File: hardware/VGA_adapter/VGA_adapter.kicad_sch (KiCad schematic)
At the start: 36 parts, among them J1 DF12NB(3.0)-30DS-0.5V(51), J2 DF12NB(3.0)-30DS-0.5V(51), J3 FPC Cable connector 1x15, U1 TXS0102DQMR

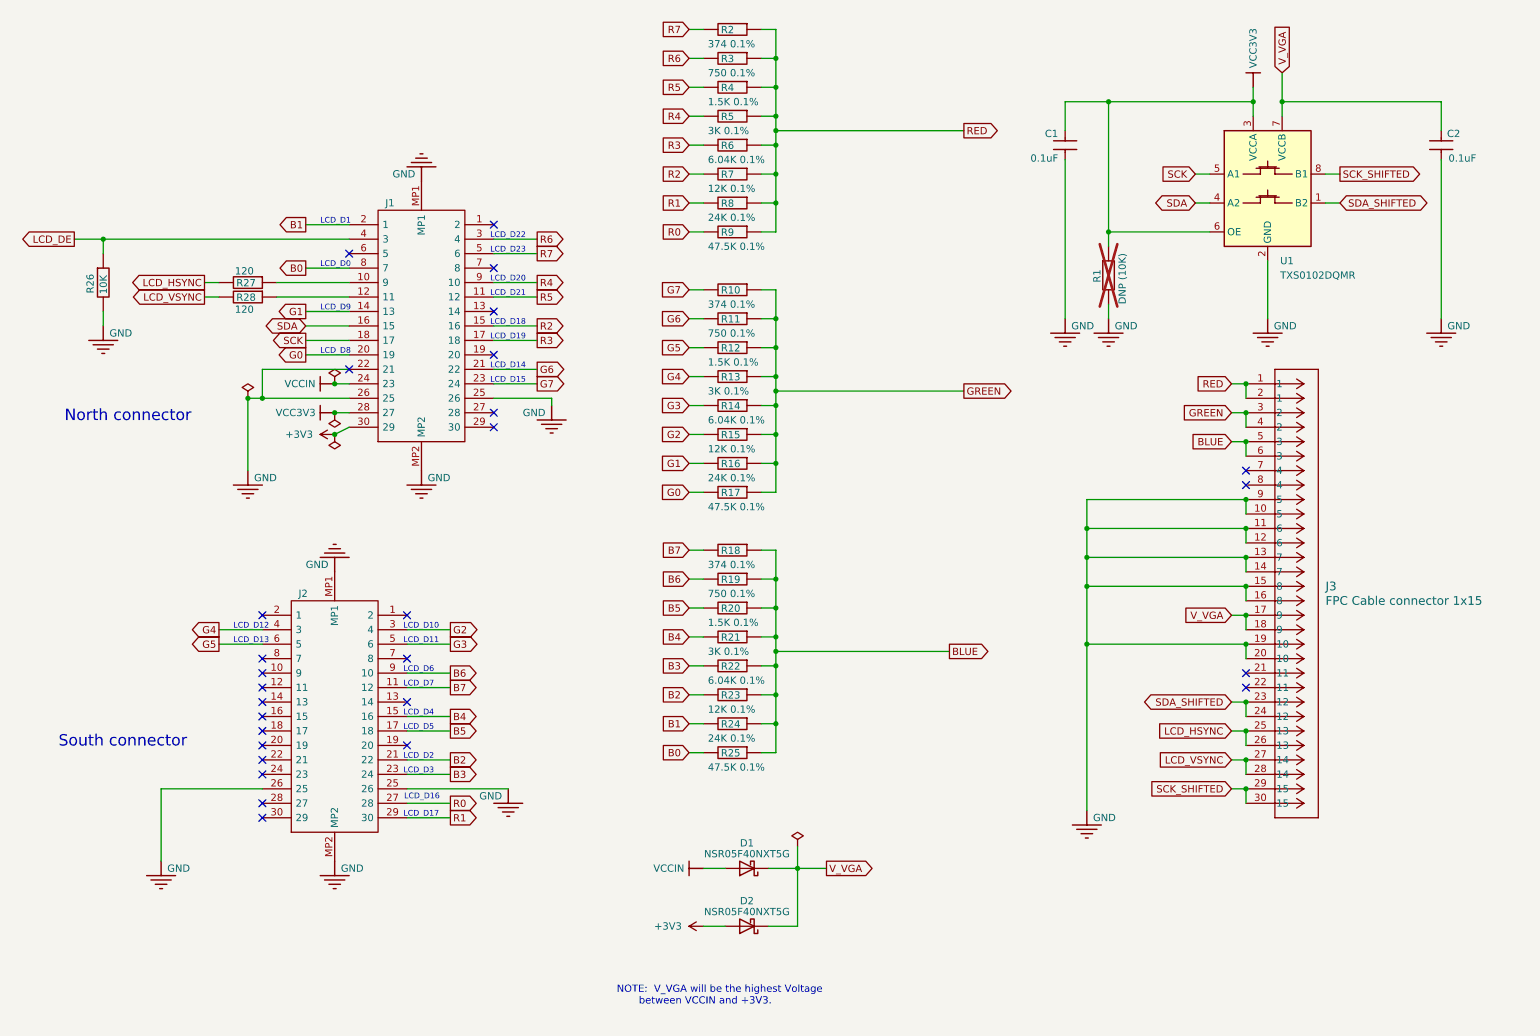
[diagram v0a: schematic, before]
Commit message: Fix transitors (correct is NMOS, fast version selected). Added charge pump. Fixed level translator pinout.
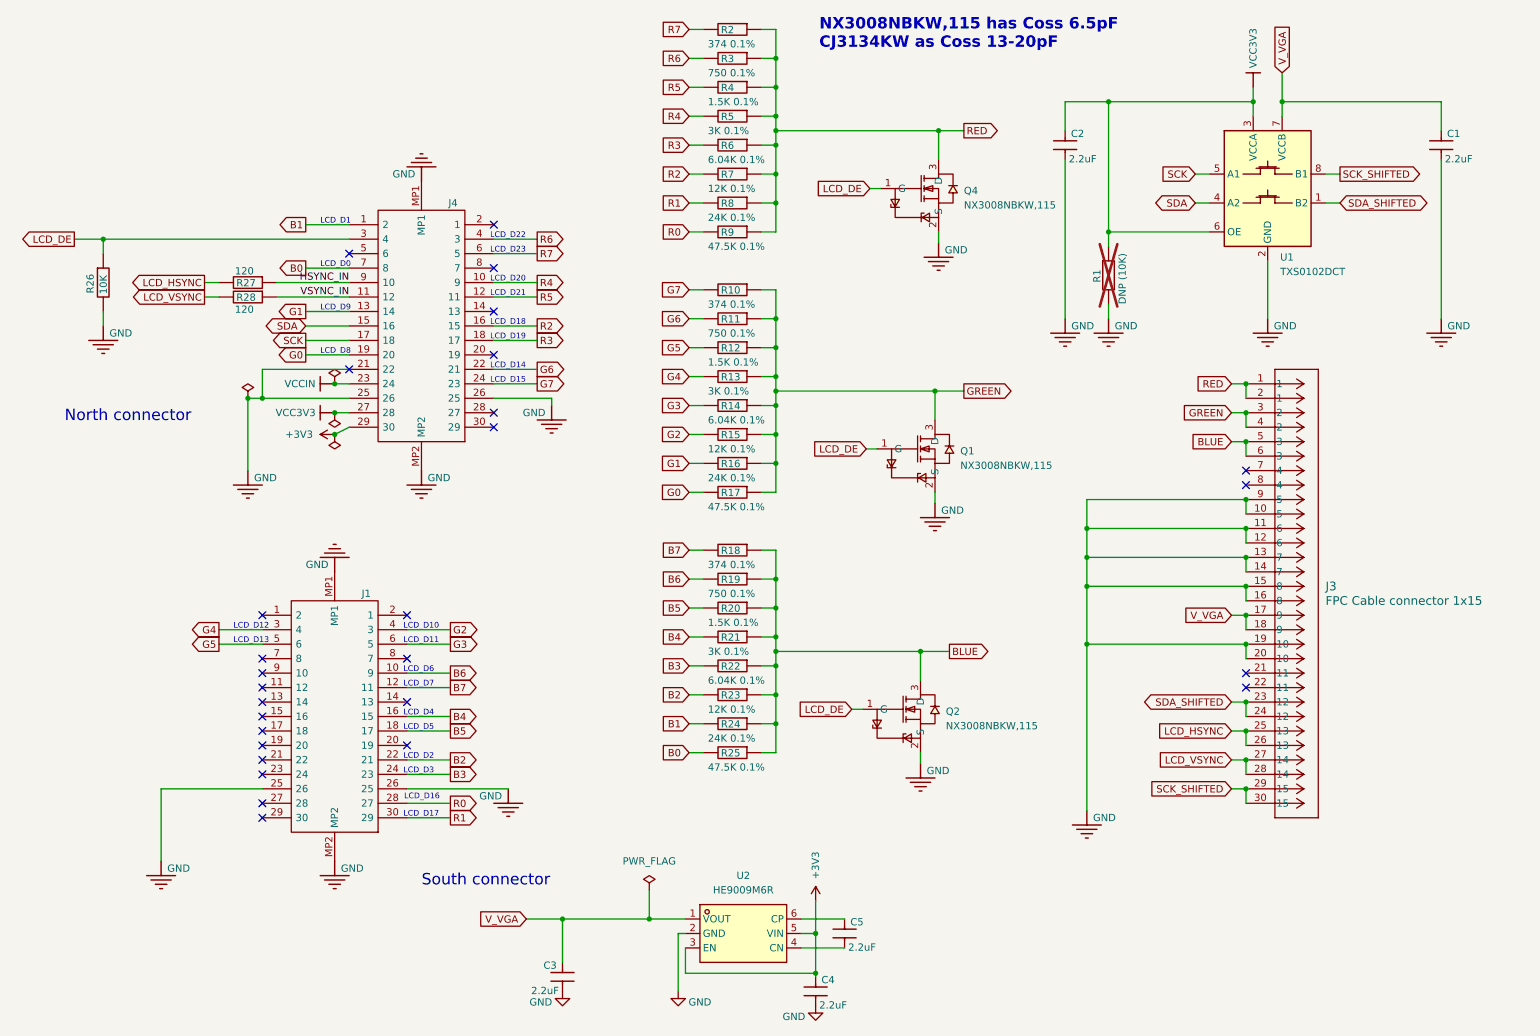
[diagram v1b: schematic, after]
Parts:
- removed D1, D2: NSR05F40NXT5G, Diode_SMD:D_0402_1005Metric, symbol Device:D_Schottky
- removed J2: DF12NB(3.0)-30DS-0.5V(51), DF12NB3030DP05V51, symbol DF12NB_3.0_-30DP-0.5V_51_:DF12NB_3.0_-30DP-0.5V_51_
- removed U1: TXS0102DQMR, Library:DQM8, symbol Logic_LevelTranslator:TXS0102DCU
- added C3, C4, C5: 2.2uF, Capacitor_SMD:C_0402_1005Metric, symbol Periph-altium-import:0_CAP
- added J4: DF12NB(3.0)-30DS-0.5V(51), easyeda2kicad:CONN-SMD_30P-P0.50_HRS_DF12NB-3.0-30DP-0.5V, symbol DF12NB_3.0_-30DP-0.5V_51_:DF12NB_3.0_-30DP-0.5V_51_
- added Q1, Q2, Q4: NX3008NBKW,115, easyeda2kicad:SOT-323-3_L2.0-W1.3-P1.30-LS2.1-BR, symbol easyeda2kicad:NX3008NBKW,115
- added U1: TXS0102DCT, Package_SO:SSOP-8_2.95x2.8mm_P0.65mm, symbol Logic_LevelTranslator:TXS0102DCT
- added U2: HE9009M6R, Package_TO_SOT_SMD:SOT-23-6, symbol easyeda2kicad:HE9009M6R
- C1, C2: value 0.1uF -> 2.2uF; footprint Library:C_0402_1005Metric -> Capacitor_SMD:C_0402_1005Metric; LCSC Part Number C60474 -> C170151
- J1: footprint DF12NB3030DP05V51 -> easyeda2kicad:CONN-SMD_30P-P0.50_HRS_DF12NB-3.0-30DP-0.5V; LCSC Part Number (none) -> C2904115
- J3: LCSC Part Number (none) -> C2922285
- R10, R18, R2: LCSC Part Number C852745 -> C2681606
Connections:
- net +3V3: now also C4.1, J4.29 (30), U2.3 (EN), U2.5 (VIN); no longer J1.30 (29)
- net B0: now also J4.7 (8); no longer J1.8 (7)
- net B1: now also J4.1 (2); no longer J1.2 (1)
- net B2: now also J1.22 (21)
- net B3: now also J1.24 (23)
- net B4: now also J1.16 (15)
- net B5: now also J1.18 (17)
- net B6: now also J1.10 (9)
- net B7: now also J1.12 (11)
- net BLUE: now also Q2.3 (D)
- net G0: now also J4.19 (20); no longer J1.20 (19)
- net G1: now also J4.13 (14); no longer J1.14 (13)
- net G2: now also J1.4 (3)
- net G3: now also J1.6 (5)
- net G4: now also J1.3 (4)
- net G5: now also J1.5 (6)
- net G6: now also J4.22 (21); no longer J1.21 (22)
- net G7: now also J4.24 (23); no longer J1.23 (24)
- net GND: now also C3.2, C4.2, J4.21 (22), J4.25 (26), J4.26 (25), J4.MP1, J4.MP2, Q1.2 (S), Q2.2 (S), Q4.2 (S), U1.2 (GND), U2.2 (GND); no longer J1.22 (21)
- net GREEN: now also Q1.3 (D)
- net LCD_DE: now also J4.3 (4), Q1.1 (G), Q2.1 (G), Q4.1 (G); no longer J1.4 (3)
- net R0: now also J1.28 (27)
- net R1: now also J1.30 (29)
- net R2: now also J4.16 (15); no longer J1.15 (16)
- net R3: now also J4.18 (17); no longer J1.17 (18)
- net R4: now also J4.10 (9); no longer J1.9 (10)
- net R5: now also J4.12 (11); no longer J1.11 (12)
- net R6: now also J4.4 (3); no longer J1.3 (4)
- net R7: now also J4.6 (5); no longer J1.5 (6)
- net RED: now also Q4.3 (D)
- net SCK: now also J4.17 (18), U1.5 (A1); no longer J1.18 (17)
- net SCK_SHIFTED: now also U1.8 (B1)
- net SDA: now also J4.15 (16), U1.4 (A2); no longer J1.16 (15)
- net SDA_SHIFTED: now also U1.1 (B2)
- net VCC3V3: now also C2.1, J4.27 (28), U1.3 (VCCA), U1.6 (OE); no longer C1.1, J1.28 (27)
- net VCCIN: now also J4.23 (24); no longer J1.24 (23)
- net V_VGA: now also C1.1, C3.1, U1.7 (VCCB), U2.1 (VOUT); no longer C2.1
- net HSYNC_IN: now reaches R27.1
- net HSYNC_IN: now also J4.9 (10); no longer J1.10 (9)
- net VSYNC_IN: now reaches R28.1
- net VSYNC_IN: now also J4.11 (12); no longer J1.12 (11)
- new net: C5.1, U2.6 (CP)
- new net: C5.2, U2.4 (CN)
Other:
- note added: "NX3008NBKW,115 has Coss 6.5pF CJ3134KW as Coss 13-20pF"
- note removed: "NOTE: V_VGA will be the highest Voltage between VCCIN and +3V3."

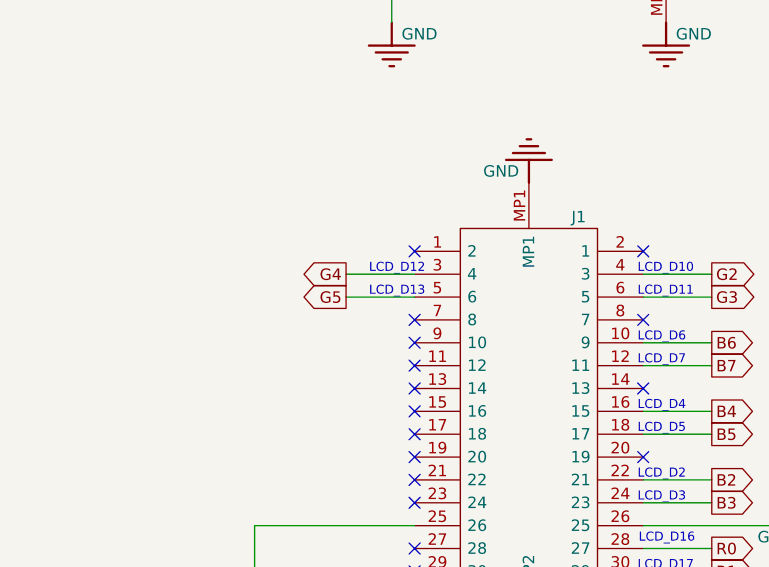
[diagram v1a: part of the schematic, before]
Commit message: fixed mixup of pins G5/G4 (3rd diff pair ODD) and DE/PCLK (3rd diff pair EVEN), now with correct polarity for diff pairs
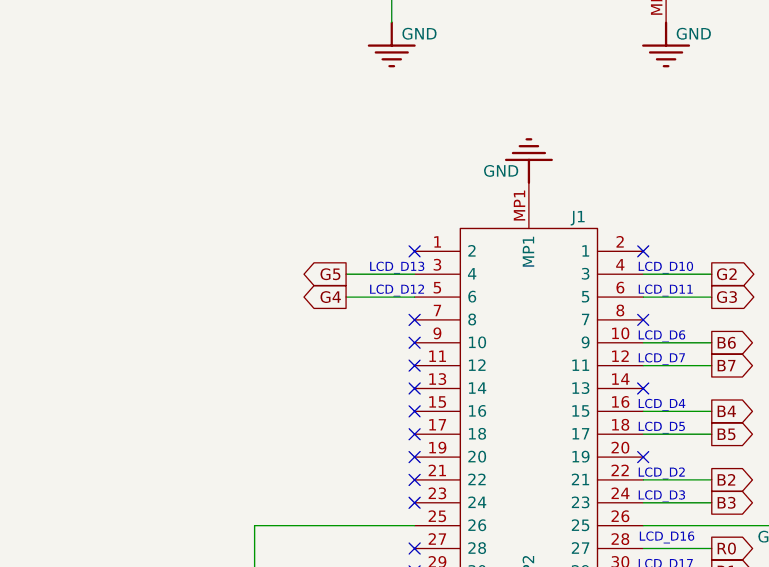
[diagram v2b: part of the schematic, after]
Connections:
- net G4: now also J1.5 (6); no longer J1.3 (4)
- net G5: now also J1.3 (4); no longer J1.5 (6)
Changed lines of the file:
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@@
+	(wire
+		(pts
+			(xy 57.15 128.27) (xy 64.77 128.27)
+		)
+		(stroke
+			(width 0.254)
+			(type default)
+		)
+	)
 	(wire
 		(pts
@@
 	(wire
 		(pts
-			(xy 57.15 128.27) (xy 64.77 128.27)
-		)
-		(stroke
-			(width 0.254)
-			(type default)
-		)
-	)
-	(wire
-		(pts
 			(xy 64.77 153.67) (xy 46.99 153.67)
 		)
@@
 	(wire
 		(pts
+			(xy 57.15 125.73) (xy 64.77 125.73)
+		)
+		(stroke
+			(width 0.254)
+			(type default)
+		)
+	)
+	(wire
+		(pts
 			(xy 152.4 96.52) (xy 154.94 96.52)
 		)
@@
 	(wire
 		(pts
-			(xy 57.15 125.73) (xy 64.77 125.73)
-		)
-		(stroke
-			(width 0.254)
-			(type default)
-		)
-	)
-	(wire
-		(pts
 			(xy 237.49 85.09) (xy 237.49 82.55)
 		)
@@
 		)
 	)
+	(text "LCD_D12"
+		(exclude_from_sim no)
+		(at 59.69 128.27 0)
+		(effects
+			(font
+				(size 1 1)
+			)
+			(justify left bottom)
+		)
+	)
 	(text "South connector"
 		(exclude_from_sim no)
@@
 		)
 	)
+	(text "LCD_D13"
+		(exclude_from_sim no)
+		(at 59.69 125.73 0)
+		(effects
+			(font
+				(size 1 1)
+			)
+			(justify left bottom)
+		)
+	)
 	(text "LCD_D11"
 		(exclude_from_sim no)
@@
 		(exclude_from_sim no)
 		(at 89.535 133.35 0)
-		(effects
-			(font
-				(size 1 1)
-			)
-			(justify left bottom)
-		)
-	)
-	(text "LCD_D13"
-		(exclude_from_sim no)
-		(at 59.69 128.27 0)
-		(effects
-			(font
-				(size 1 1)
-			)
-			(justify left bottom)
-		)
-	)
-	(text "LCD_D12"
-		(exclude_from_sim no)
-		(at 59.69 125.73 0)
 		(effects
 			(font
@@
 		)
 	)
+	(global_label "G5"
+		(shape output)
+		(at 57.15 125.73 180)
+		(fields_autoplaced yes)
+		(effects
+			(font
+				(size 1.27 1.27)
+			)
+			(justify right)
+		)
+		(property "Intersheetrefs" "${INTERSHEET_REFS}"
+			(at 51.6853 125.73 0)
+			(effects
+				(font
+					(size 1.27 1.27)
+				)
+				(justify right)
+				(hide yes)
+			)
+		)
+	)
 	(global_label "R7"
 		(shape input)
@@
 		(property "Intersheetrefs" "${INTERSHEET_REFS}"
 			(at 134.2353 20.32 0)
+			(effects
+				(font
+					(size 1.27 1.27)
+				)
+				(justify right)
+				(hide yes)
+			)
+		)
+	)
+	(global_label "G4"
+		(shape output)
+		(at 57.15 128.27 180)
+		(fields_autoplaced yes)
+		(effects
+			(font
+				(size 1.27 1.27)
+			)
+			(justify right)
+		)
+		(property "Intersheetrefs" "${INTERSHEET_REFS}"
+			(at 51.6853 128.27 0)
 			(effects
 				(font
@@
 		)
 	)
-	(global_label "G4"
-		(shape output)
-		(at 57.15 125.73 180)
-		(fields_autoplaced yes)
-		(effects
-			(font
-				(size 1.27 1.27)
-			)
-			(justify right)
-		)
-		(property "Intersheetrefs" "${INTERSHEET_REFS}"
-			(at 51.6853 125.73 0)
-			(effects
-				(font
-					(size 1.27 1.27)
-				)
-				(justify right)
-				(hide yes)
-			)
-		)
-	)
 	(global_label "R4"
 		(shape output)
@@
 				(hide yes)
 			)
-		)
-	)
-	(global_label "G5"
-		(shape output)
-		(at 57.15 128.27 180)
-		(fields_autoplaced yes)
-		(effects
-			(font
-				(size 1.27 1.27)
-			)
-			(justify right)
-		)
-		(property "Intersheetrefs" "${INTERSHEET_REFS}"
-			(at 51.6853 128.27 0)
-			(effects
-				(font
-					(size 1.27 1.27)
-				)
-				(justify right)
-				(hide yes)
-			)

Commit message: correct footprint of VGA adapter's level translator
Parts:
- removed U1: TXS0102DCT, Package_SO:SSOP-8_2.95x2.8mm_P0.65mm, symbol Logic_LevelTranslator:TXS0102DCT
- added U1: TXS0102DCU, Package_SO:VSSOP-8_2.3x2mm_P0.5mm, symbol Logic_LevelTranslator:TXS0102DCU
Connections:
- net GND: now also U1.2 (GND)
- net SCK: now also U1.5 (A1)
- net SCK_SHIFTED: now also U1.8 (B1)
- net SDA: now also U1.4 (A2)
- net SDA_SHIFTED: now also U1.1 (B2)
- net VCC3V3: now also U1.3 (VCCA), U1.6 (OE)
- net V_VGA: now also U1.7 (VCCB)
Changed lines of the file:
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@@
+	)
+	(symbol
+		(lib_id "Logic_LevelTranslator:TXS0102DCU")
+		(at 241.3 48.26 0)
+		(unit 1)
+		(exclude_from_sim no)
+		(in_bom yes)
+		(on_board yes)
+		(dnp no)
+		(fields_autoplaced yes)
+		(property "Reference" "U1"
+			(at 243.4941 60.96 0)
+			(effects
+				(font
+					(size 1.27 1.27)
+				)
+				(justify left)
+			)
+		)
+		(property "Value" "TXS0102DCU"
+			(at 243.4941 63.5 0)
+			(effects
+				(font
+					(size 1.27 1.27)
+				)
+				(justify left)
+			)
+		)
+		(property "Footprint" "Package_SO:VSSOP-8_2.3x2mm_P0.5mm"
+			(at 241.3 62.23 0)
+			(effects
+				(font
+					(size 1.27 1.27)
+				)
+				(hide yes)
+			)
+		)
+		(property "Datasheet" "http://www.ti.com/lit/gpn/txs0102"
+			(at 241.3 48.768 0)
+			(effects
+				(font
+					(size 1.27 1.27)
+				)
+				(hide yes)
+			)
+		)
+		(property "Description" "2-Bit Bidirectional Voltage-Level Shifter for Open-Drain and Push-Pull Application, VSSOP-8"
+			(at 241.3 48.26 0)
+			(effects
+				(font
+					(size 1.27 1.27)
+				)
+				(hide yes)
+			)
+		)
+		(property "LCSC Part Number" "C53434"
+			(at 241.3 48.26 0)
+			(effects
+				(font
+					(size 1.27 1.27)
+				)
+				(hide yes)
+			)
+		)
+		(pin "7"
+		)
+		(pin "6"
+		)
+		(pin "5"
+		)
+		(pin "4"
+		)
+		(pin "3"
+		)
+		(pin "2"
+		)
+		(pin "1"
+		)
+		(pin "8"
+		)
+		(instances
+			(project "VGA_adapter"
+				(path "/971d21cc-a5c8-4932-ad62-f68d6b0e4b00"
+					(reference "U1")
+					(unit 1)
+				)
+			)
+		)
 	)
 	(symbol
@@
 					(unit 1)
 				)
-			)
-		)
-	)
-	(symbol
-		(lib_id "Logic_LevelTranslator:TXS0102DCT")
-		(at 241.3 48.26 0)
-		(unit 1)
-		(exclude_from_sim no)
-		(in_bom yes)
-		(on_board yes)
-		(dnp no)
-		(fields_autoplaced yes)
-		(property "Reference" "U1"
-			(at 243.4941 60.325 0)
-			(effects
-				(font
-					(size 1.27 1.27)
-				)
-				(justify left)
-			)
-		)
-		(property "Value" "TXS0102DCT"
-			(at 243.4941 62.865 0)
-			(effects
-				(font
-					(size 1.27 1.27)
-				)
-				(justify left)
-			)
-		)
-		(property "Footprint" "Package_SO:SSOP-8_2.95x2.8mm_P0.65mm"
-			(at 241.3 62.23 0)
-			(effects
-				(font
-					(size 1.27 1.27)
-				)
-				(hide yes)
-			)
-		)
-		(property "Datasheet" "http://www.ti.com/lit/gpn/txs0102"
-			(at 241.3 48.768 0)
-			(effects
-				(font
-					(size 1.27 1.27)
-				)
-				(hide yes)
-			)
-		)
-		(property "Description" "2-Bit Bidirectional Voltage-Level Shifter for Open-Drain and Push-Pull Application, SSOP-8"
-			(at 241.3 48.26 0)
-			(effects
-				(font
-					(size 1.27 1.27)
-				)
-				(hide yes)
-			)
-		)
-		(pin "2"
-		)
-		(pin "1"
-		)
-		(pin "3"
-		)
-		(pin "4"
-		)
-		(pin "5"
-		)
-		(pin "6"
-		)
-		(pin "7"
-		)
-		(pin "8"
-		)
-		(instances
-			(project "VGA_adapter"
-				(path "/971d21cc-a5c8-4932-ad62-f68d6b0e4b00"
-					(reference "U1")
-					(unit 1)
-				)
